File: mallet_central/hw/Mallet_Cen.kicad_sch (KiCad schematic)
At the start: 23 parts, among them J1 Barrel_Jack_Switch_Pin3Ring, J2 Conn_01x04, J3 Conn_01x08, J4 Conn_01x04, U1 MT2492, U2 STM32G030F6Px, U3 LTC4311CSC6#TRPBF

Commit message: Revise central module hardware design
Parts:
- removed J3: Conn_01x08, Mallet_Cen_footprints:SMD_Module_P1.27_1x08, symbol Connector_Generic:Conn_01x08
- added J3: Conn_02x04_Odd_Even, Connector_PinSocket_2.54mm:PinSocket_2x04_P2.54mm_Vertical, symbol Connector_Generic:Conn_02x04_Odd_Even
- J4: value Conn_01x04 -> Conn_01x05; footprint Connector_PinHeader_2.00mm:PinHeader_1x04_P2.00mm_Vertical -> Connector_PinHeader_2.00mm:PinHeader_1x05_P2.00mm_Vertical; symbol Connector_Generic:Conn_01x04 -> Connector_Generic:Conn_01x05
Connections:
- net ACT_LED: now also U2.15 (PB0/PB1/PB2/PA8); no longer U2.2 (PC14/PB9)
- net GND: now also J3.1 (Pin_1)
- net I2C2_SCL: now also J4.4 (Pin_4); no longer J4.3 (Pin_3)
- net I2C2_SDA: now also J4.5 (Pin_5); no longer J4.4 (Pin_4)
- net SPI1_MISO: now also J3.7 (Pin_7)
- net SPI1_MOSI: now also J3.6 (Pin_6)
- net VBUS: now also J4.1 (Pin_1)
- net VDD: now also J4.3 (Pin_3), J3.2 (Pin_2); no longer J4.1 (Pin_1)
- net nRF_CE: now also U2.2 (PC14/PB9), J3.3 (Pin_3); no longer U2.7 (PA0)
- net nRF_IRQ: now reaches U2.14 (PA7)
- net nRF_IRQ: now also J3.8 (Pin_8)
- net SPI1_CK renamed SPI1_SCK
- net SPI1_SCK: now also J3.5 (Pin_5)
- net SPI1_CSx: no longer names the net of U2.10 (PA3)
- new net nRF_CS: J3.4 (Pin_4), U2.7 (PA0)
- no-connect marks 10 -> 8
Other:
- note added: "GPIO IN"
- note added: "GPIO PPO"
- note added: "P2.54 2x04"
- note removed: "GPIO"
- note removed: "P1.27 1x08"

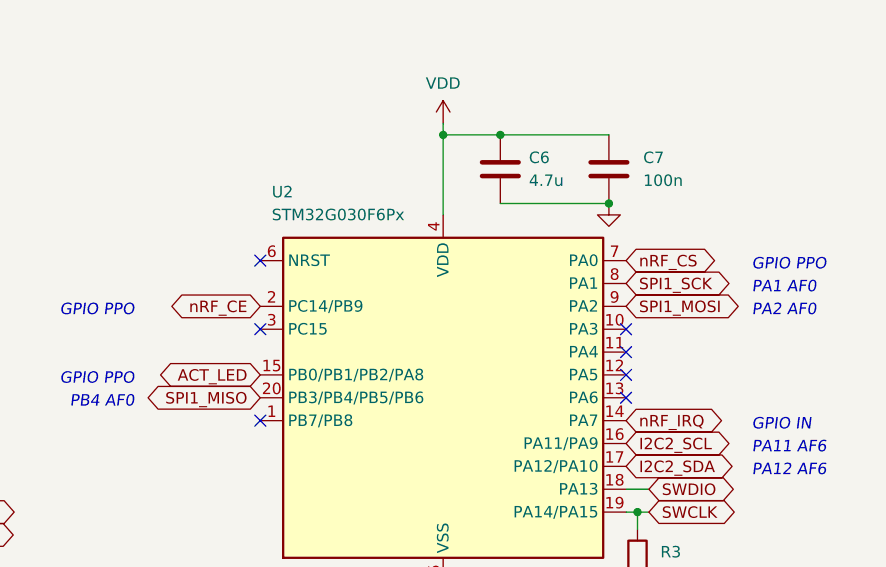
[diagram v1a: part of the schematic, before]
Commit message: Fix incorrect pin assignment for external RF module; submit for fab
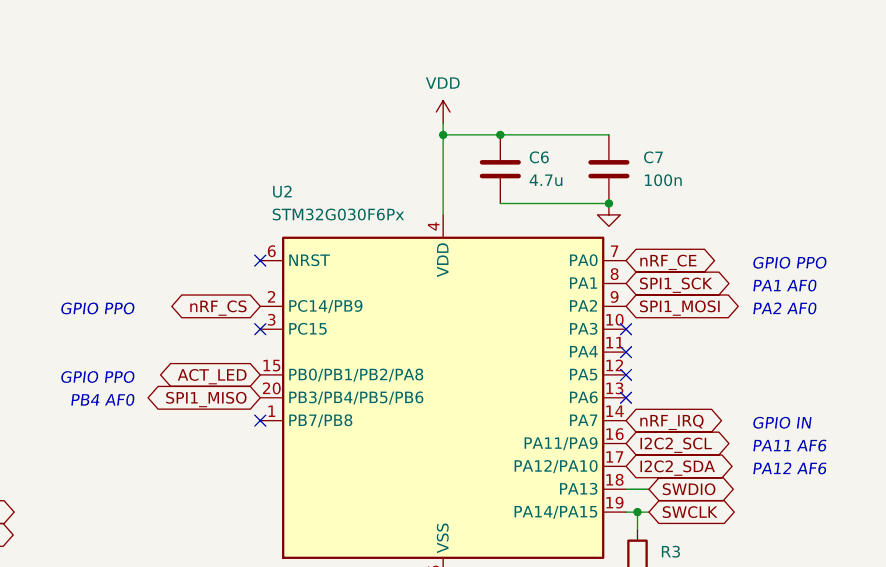
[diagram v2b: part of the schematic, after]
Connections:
- net nRF_CE: now also U2.7 (PA0); no longer U2.2 (PC14/PB9)
- net nRF_CS: now also U2.2 (PC14/PB9); no longer U2.7 (PA0)
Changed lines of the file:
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@@
     )
   )
-  (global_label "nRF_CE" (shape bidirectional) (at 85.725 95.885 180) (fields_autoplaced)
+  (global_label "nRF_CS" (shape bidirectional) (at 85.725 95.885 180) (fields_autoplaced)
     (effects (font (size 1.27 1.27)) (justify right))
-    (property "Intersheetrefs" "${INTERSHEET_REFS}" (at 74.7343 95.885 0)
+    (property "Intersheetrefs" "${INTERSHEET_REFS}" (at 74.6738 95.885 0)
       (effects (font (size 1.27 1.27)) (justify right) hide)
     )
@@
     )
   )
-  (global_label "nRF_CS" (shape bidirectional) (at 126.365 90.805 0) (fields_autoplaced)
+  (global_label "nRF_CE" (shape bidirectional) (at 126.365 90.805 0) (fields_autoplaced)
     (effects (font (size 1.27 1.27)) (justify left))
-    (property "Intersheetrefs" "${INTERSHEET_REFS}" (at 137.4162 90.805 0)
+    (property "Intersheetrefs" "${INTERSHEET_REFS}" (at 137.3557 90.805 0)
       (effects (font (size 1.27 1.27)) (justify left) hide)
     )
